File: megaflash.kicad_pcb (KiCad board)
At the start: 2 copper layers, 73.8 x 56.5 mm, 25 parts, among them J1 ROM7, J2 ROM0, J3 CPC_EXTPORT, SW1 READ/WRITE, U1 74LS374, U2 74LS32, U3 74LS32, U4 74LS02, U5 74LS20, U6 W29C040

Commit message: Fixed scrambled latch inputs. Board mostly routed.
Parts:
- moved C5 69.2 mm to (117.3, 93.9)
- moved C6 69.2 mm to (107.3, 93.9)
- moved C7 69.2 mm to (97.3, 93.9)
- moved C3 43.1 mm to (88.3, 93.6)
- moved C4 43.1 mm to (78.3, 93.6)
- moved R1 22.1 mm to (101.2, 104.0), turned to 90 degrees
- moved R2 13.7 mm to (134.0, 100.1), turned to 270 degrees
- moved R4 8.36 mm to (126.2, 100.1), turned to 90 degrees
- moved LD1 7.91 mm to (130.4, 99.6), turned to 90 degrees
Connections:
- net /L7 renamed /A21
- C3 pad 1: N-0000046 (its old number) -> VCC
- C3 pad 2: N-0000045 -> GND
- C4 pad 1: N-0000047 (its old number) -> VCC
- C4 pad 2: N-0000048 (its old number) -> GND
- C5 pad 1: N-0000049 -> VCC
- C5 pad 2: N-0000050 (its old number) -> GND
- C6 pad 1: N-0000051 (its old number) -> VCC
- C6 pad 2: N-0000052 -> GND
- C7 pad 1: N-0000053 (its old number) -> VCC
- C7 pad 2: N-0000054 (its old number) -> GND
- D2 pad 1: /L0 -> /A20
- D2 pad 2: /L0+L7 -> /A20+A21
- D3 pad 2: /L0+L7 -> /A20+A21
- R3 pad 2: /L0+L7 -> /A20+A21
- U1 pad 12: /A15 -> /A18
- U1 pad 15: /A17 -> /A19
- U1 pad 16: /L6 -> /A20
- U1 pad 2: /L0 -> /A14
- U1 pad 5: /A18 -> /A15
- U1 pad 9: /A14 -> /A17
- U4 pad 2: /L0+L7 -> /A20+21
- U4 pad 3: /L6 -> /A19
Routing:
- net N-0000047: track 0.00 -> 72.4 mm
- net /A17: track 107.2 -> 36.3 mm, vias 4 -> 2
- net /A18: track 134.3 -> 78.5 mm
- net /L0+L7: track 53.5 -> 0.00 mm, vias 2 -> 0
- net /L6: track 50.9 -> 0.00 mm, vias 2 -> 0
- net /A14: track 64.4 -> 38.6 mm, vias 2 -> 0
- net /L0: track 13.6 -> 0.00 mm
- net N-0000046: track 0.00 -> 8.62 mm
- net VCC: track 246.6 -> 254.7 mm, vias 8 -> 9
- net GND: track 125.3 -> 130.9 mm, vias 5 -> 6
- net (no net): track 0.00 -> 5.39 mm, vias 0 -> 4
- net /A20+A21: track 0.00 -> 4.11 mm
- net N-0000051: track 0.00 -> 3.19 mm
- net /ROMDIS: track 43.2 -> 46.3 mm
- net /A15: track 69.1 -> 66.3 mm
- added copper zone on B.Cu, net GND
- added copper zone on F.Cu, net GND

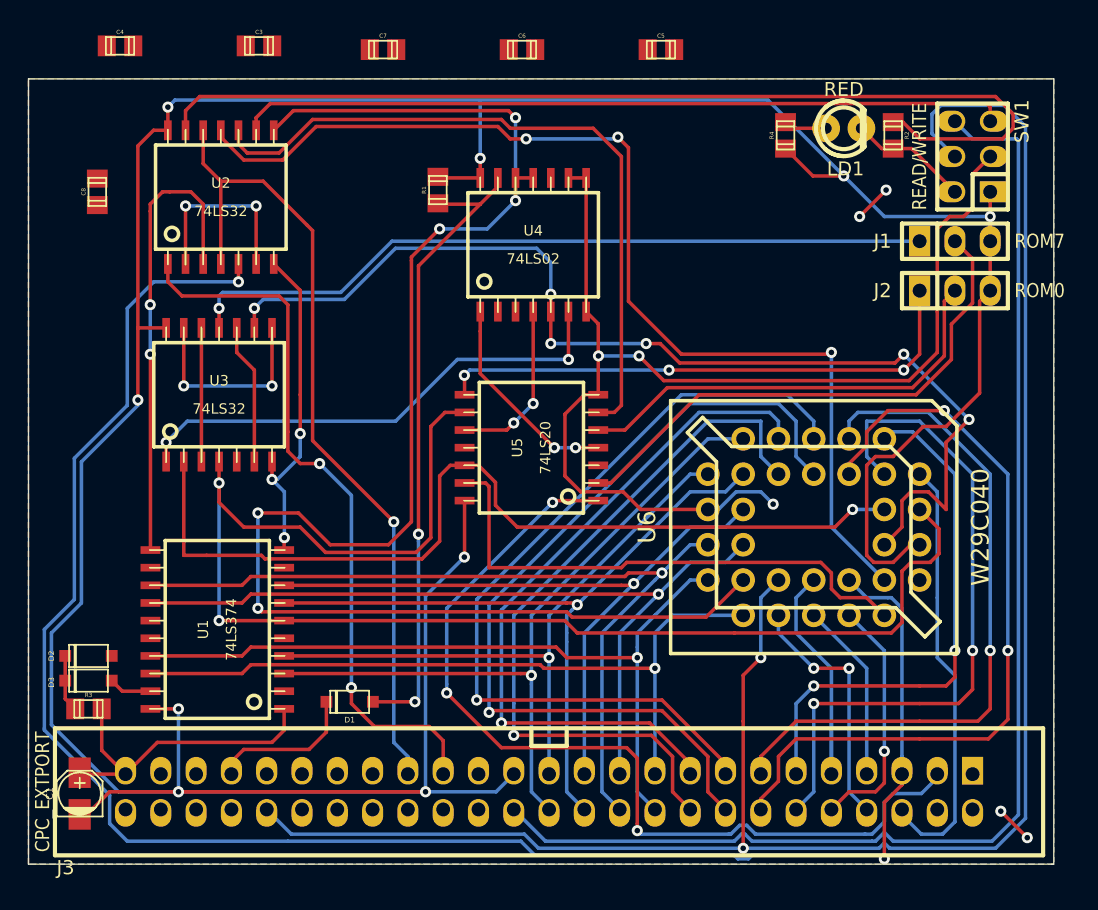
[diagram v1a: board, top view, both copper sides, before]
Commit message: Completed v1 schematic and layout using XC9536 cpld.
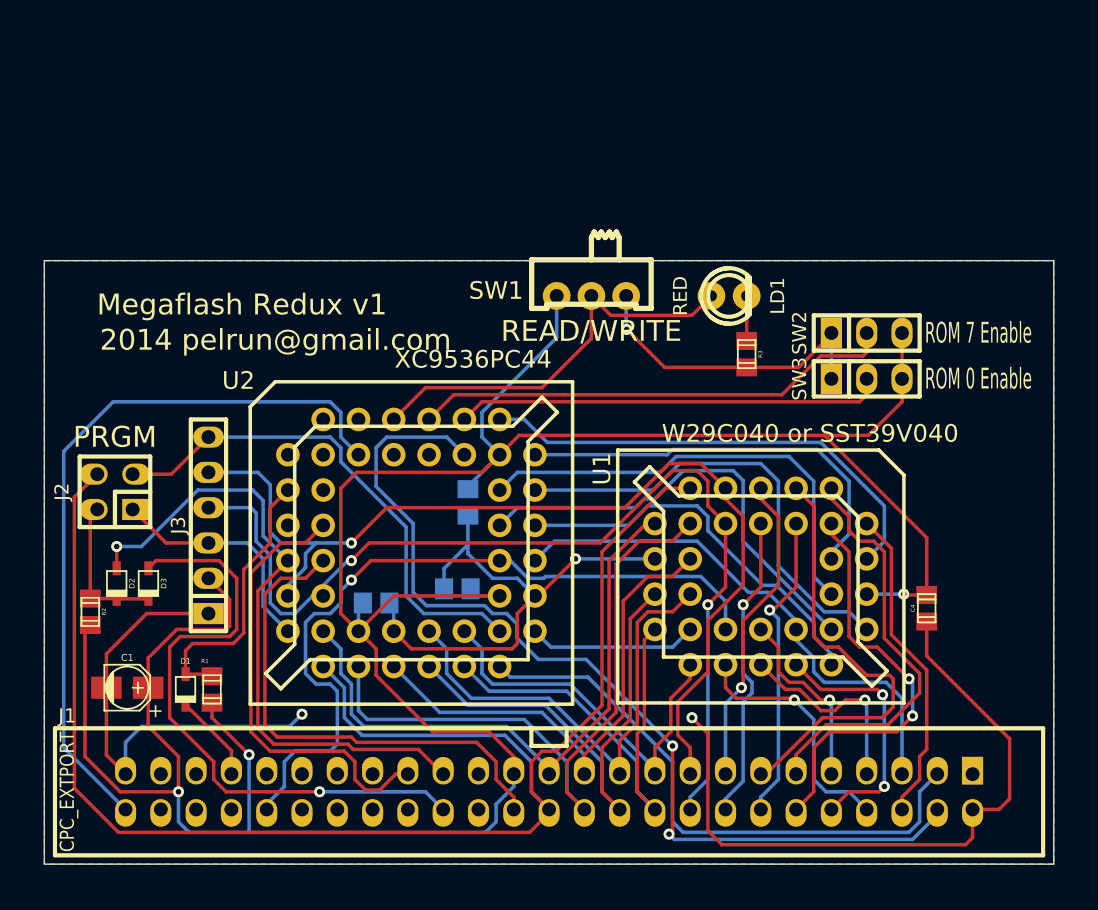
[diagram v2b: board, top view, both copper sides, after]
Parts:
- removed C6, C7, C8: 100n, c_0805
- removed the J1 at (138.4, 107.7)
- removed the R3 at (76.1, 141.4)
- removed R4: 1K, r_0805
- removed the U1 at (85.3, 135.6)
- removed U3: 74LS32, soic-14
- removed U4: 74LS02, soic-14
- removed U5: 74LS20, soic-14
- added C4: 10n, c_0805, F.Cu at (136.4, 134.1)
- added J3: JTAG, pin_strip_6, F.Cu at (84.7, 128.1)
- added R2: 10k, r_0805, F.Cu at (76.2, 134.4)
- added SW2: ROM0ENABLE, pin_strip_3, F.Cu at (132.1, 114.3)
- added SW3: ROM7ENABLE, pin_strip_3, F.Cu at (132.1, 117.6)
- C2: renamed from C3; value 100n -> 10n; moved to B.Cu
- C3: renamed from C4; value 100n -> 10n; moved to B.Cu
- C5: value 100n -> 10n; moved to B.Cu
- D1, D2, D3: footprint sod123 -> sod323
- J2: value ROM0 -> PROG; footprint pin_strip_3 -> pin_strip_2x2
- R3: renamed from R2; value 220 -> 1k
- SW1: value READ/WRITE -> ~READ~/WRITE; footprint pin_socket_3x2 -> switch_mmp122-r
- U1: renamed from U6; value W29C040 -> W29C040 or SST39V040
- U2: value 74LS32 -> XC9536PC44; footprint soic-14 -> plcc44_pth-skt
- moved J2 62.2 mm to (78.0, 125.7), turned to 90 degrees
- moved C3 44.1 mm to (96.8, 133.7), turned to 180 degrees
- moved C5 41.5 mm to (102.6, 132.7)
- moved R1 39.4 mm to (85.0, 140.0), turned to 270 degrees
- moved C2 36.1 mm to (103.4, 126.5), turned to 90 degrees
- moved SW1 29.2 mm to (112.3, 111.6), turned to 180 degrees
- moved U2 28.4 mm to (99.3, 129.4), turned to 180 degrees
- moved R3 19.0 mm to (123.4, 115.8)
- moved LD1 14.6 mm to (122.2, 111.6)
- moved D1 11.8 mm to (83.1, 140.0), turned to 270 degrees
- moved C1 8.36 mm to (78.9, 139.8), turned to 0 degrees
- moved D3 8.21 mm to (80.4, 132.3), turned to 270 degrees
- moved D2 5.59 mm to (78.1, 132.3), turned to 270 degrees
- moved U1 5.21 mm to (124.5, 131.8)
- renumbered J3 to J1
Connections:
- C1 pad 1: GND -> VCC
- C1 pad 2: VCC -> GND
- D2 pad 1: /A20 -> /~IORQ
- D2 pad 2: /A20+A21 -> N-0000033
- D3 pad 1: /A21 -> /~RD
- D3 pad 2: /A20+A21 -> N-0000033
- J1 pad 32: N-0000069 -> /~RD
- J1 pad 4: N-0000067 -> /A14EXT
- J1 pad 50: N-0000077 -> /CLK
- J2 pad 1: /~ROM7DECODE -> N-0000029
- J2 pad 2: /~ROM0SEL -> N-0000033
- J2 pad 3: VCC -> N-0000036
- LD1 pad 1: N-0000051 (its old number) -> /~RD~WR
- LD1 pad 2: N-0000046 (its old number) -> N-0000064
- R3 pad 1: N-0000046 (its old number) -> GND
- R3 pad 2: N-0000047 (its old number) -> N-0000064
- SW1 pad 1: VCC -> GND
- SW1 pad 2: N-0000046 (its old number) -> /~RD~WR
- SW1 pad 3: GND -> VCC
- U2 pad 1: /~IORQ -> N-0000071
- U2 pad 10: N-0000048 (its old number) -> GND
- U2 pad 11: /~WREN -> N-0000066
- U2 pad 13: N-0000047 (its old number) -> /~IORQ
- U2 pad 14: VCC -> /~MREQ
- U2 pad 2: N-0000054 -> /~RD~WR
- U2 pad 4: /~WR -> N-0000070
- U2 pad 5: /A13 -> /CLK
- U2 pad 6: N-0000054 -> N-0000069
- U2 pad 7: GND -> N-0000068
- U2 pad 8: /~CE -> N-0000067
- U2 pad 9: N-0000019 -> /ROMDIS
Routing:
- net /~CE: track 111.1 -> 12.2 mm, vias 5 -> 0
- net /A13: track 133.2 -> 38.6 mm, vias 2 -> 0
- net /~ROMEN: track 138.5 -> 54.5 mm, vias 2 -> 1
- net N-0000047 (its old number): track 72.4 -> 0.00 mm
- net /A14EXT: track 0.00 -> 69.6 mm, vias 0 -> 2
- net /A16: track 101.3 -> 34.6 mm, vias 2 -> 0
- net /D0: track 52.4 -> 112.7 mm, vias 1 -> 0
- net /~MREQ: track 92.7 -> 36.3 mm
- net N-0000019: track 55.3 -> 0.00 mm
- net /~ROM0DECODE: track 54.4 -> 0.00 mm, vias 1 -> 0
- net /CLK: track 0.00 -> 52.9 mm
- net N-0000048 (its old number): track 50.7 -> 0.00 mm
- net VCC: track 254.7 -> 207.1 mm, vias 9 -> 3
- net /A18: track 78.5 -> 33.0 mm, vias 6 -> 0
- net /~WREN: track 77.5 -> 32.8 mm, vias 3 -> 0
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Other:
- board size 73.8 x 56.5 mm -> 72.6 x 43.4 mm
- board text added: "+"
- board text added: "2014 pelrun@gmail.com"
- board text added: "Megaflash Redux v1"
- board text added: "PRGM"
- board text added: "READ/WRITE"
- board text added: "ROM 0 Enable"
- board text added: "ROM 7 Enable"

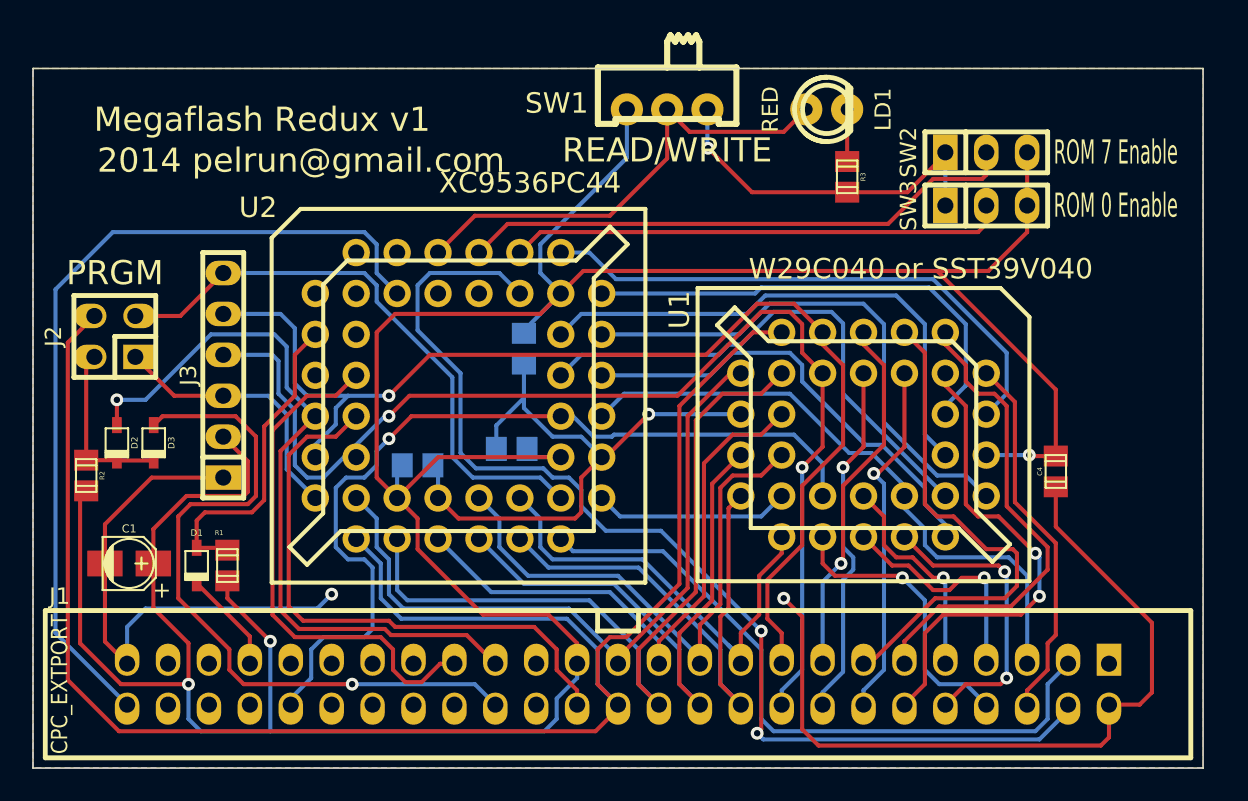
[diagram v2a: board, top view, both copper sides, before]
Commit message: Replaced switch with one that's available from digikey.
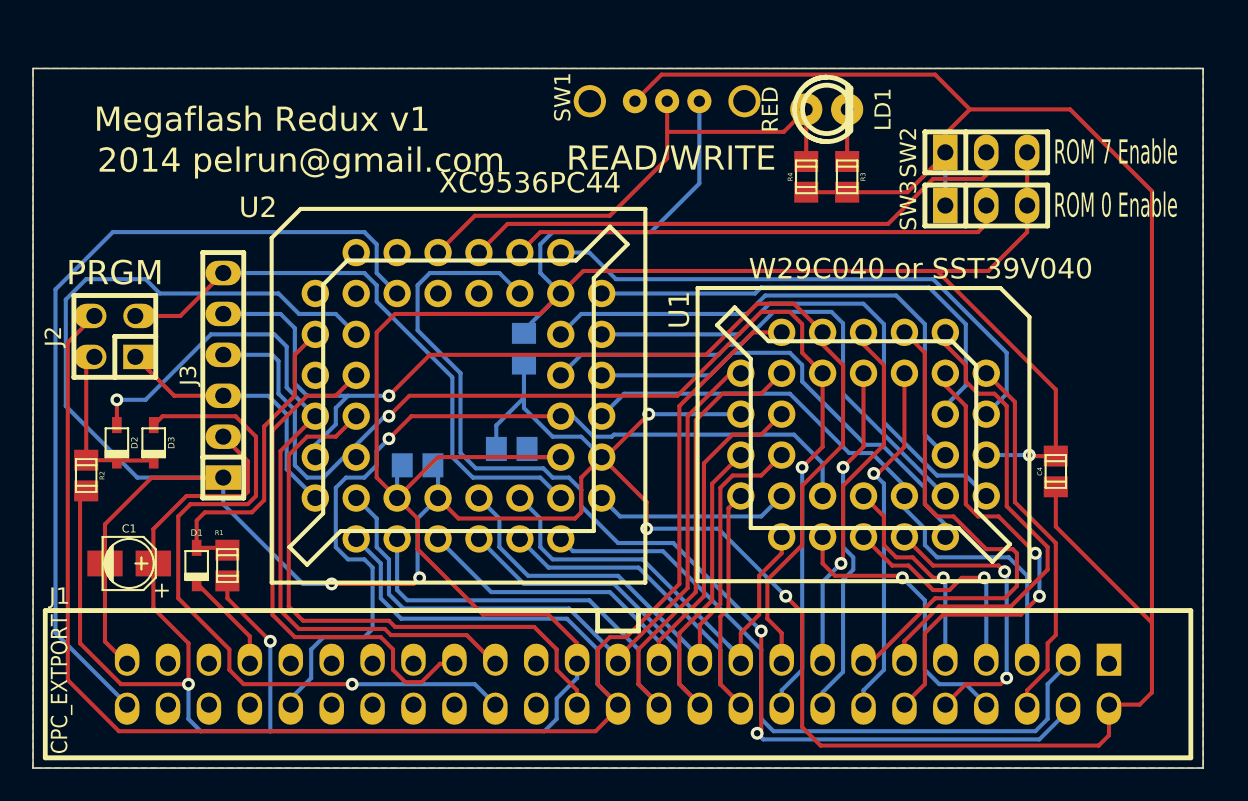
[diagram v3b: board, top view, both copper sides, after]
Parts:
- added R4: 10k, r_0805, F.Cu at (120.9, 115.8)
- R1: value 1K -> 1k
- SW1: footprint switch_mmp122-r -> switch-eg1213-spdt
- moved SW1 0.51 mm to (112.3, 111.1), turned to 0 degrees
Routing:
- net GND: track 143.0 -> 259.1 mm, vias 4 -> 5
- net VCC: track 207.1 -> 213.0 mm
- net /~RD~WR: track 29.5 -> 32.7 mm

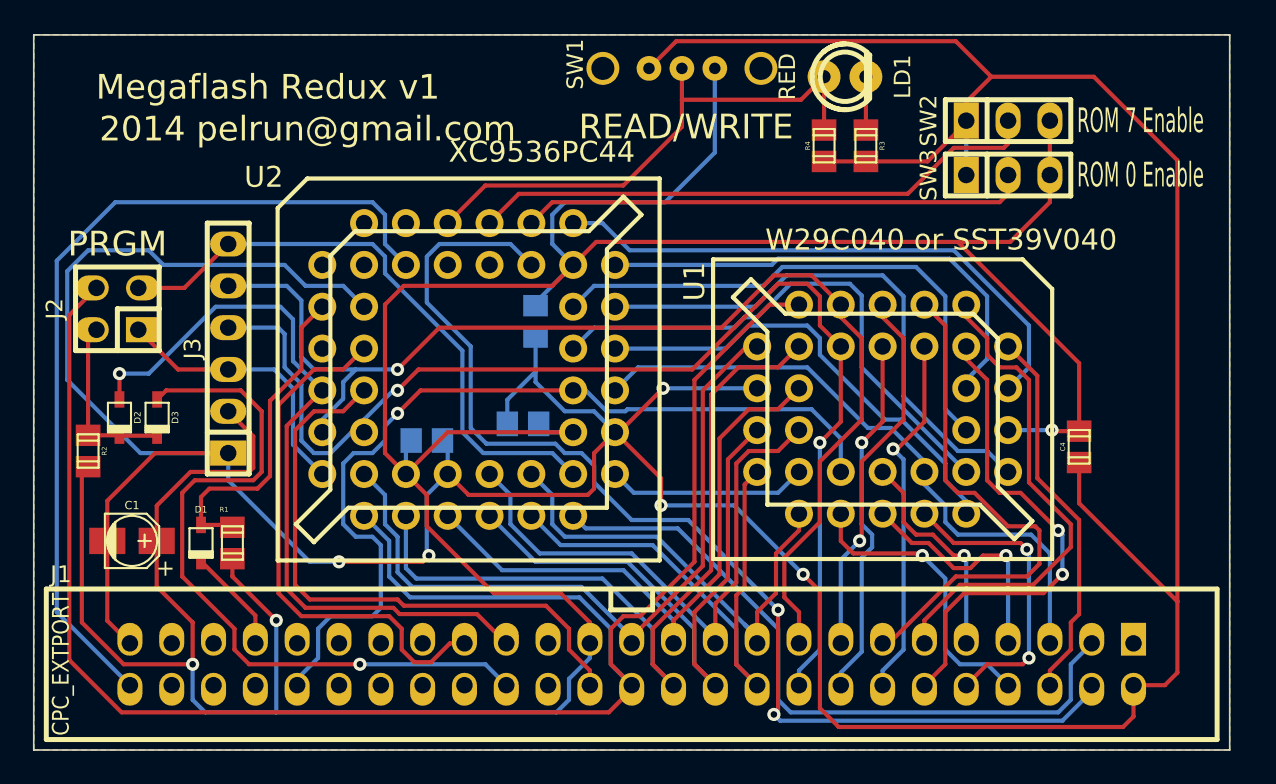
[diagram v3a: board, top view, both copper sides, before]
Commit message: Switch to the 3.3v XC9536XL (since the 5v XC9536 is unavailable)
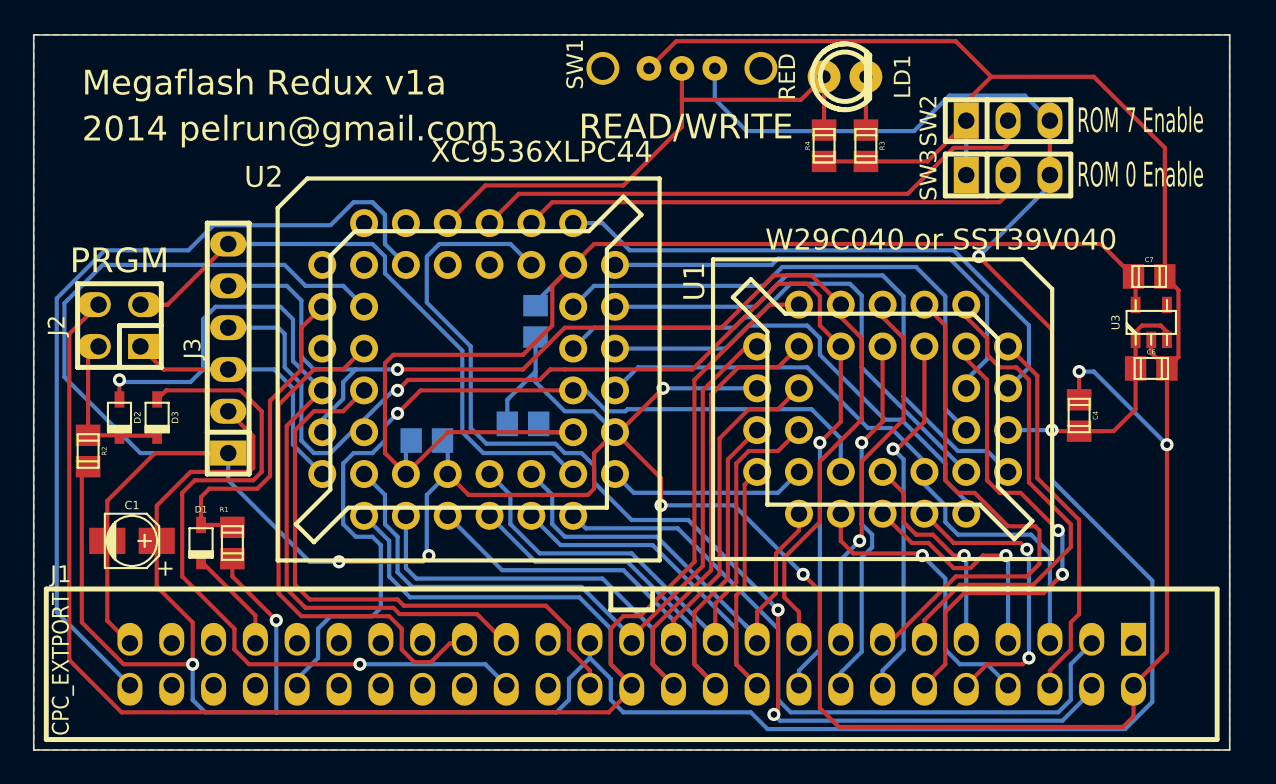
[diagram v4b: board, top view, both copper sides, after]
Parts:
- added C6: 1u, c_0805, F.Cu at (140.8, 129.3)
- added C7: 1u, c_0805, F.Cu at (140.7, 123.8)
- added U3: TLV70033, sot23-5, F.Cu at (140.8, 126.6)
- U2: value XC9536PC44 -> XC9536XLPC44
- moved C4 1.91 mm to (136.4, 132.2), turned to 270 degrees
- moved J2 1.02 mm to (78.1, 126.7)
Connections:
- C2 pad 1: VCC -> +3.3V
- C3 pad 1: VCC -> +3.3V
- C5 pad 1: VCC -> +3.3V
- U2 pad 21: VCC -> +3.3V
- U2 pad 32: VCC -> +3.3V
- U2 pad 41: VCC -> +3.3V
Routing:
- net +3.3V: track 0.00 -> 78.8 mm
- net VCC: track 213.0 -> 199.4 mm, vias 3 -> 4
- net GND: track 259.1 -> 256.5 mm, vias 5 -> 7
- net /~IORQ: track 46.8 -> 48.5 mm
- net /CLK: track 52.9 -> 54.4 mm
- net /D0: track 112.7 -> 111.7 mm
- net N-0000031: track 10.8 -> 9.86 mm
- net N-0000034: track 16.8 -> 16.3 mm
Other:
- board text added: "Megaflash Redux v1a"
- board text removed: "Megaflash Redux v1"
